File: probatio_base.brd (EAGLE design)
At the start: 50 x 50 mm, 12 parts

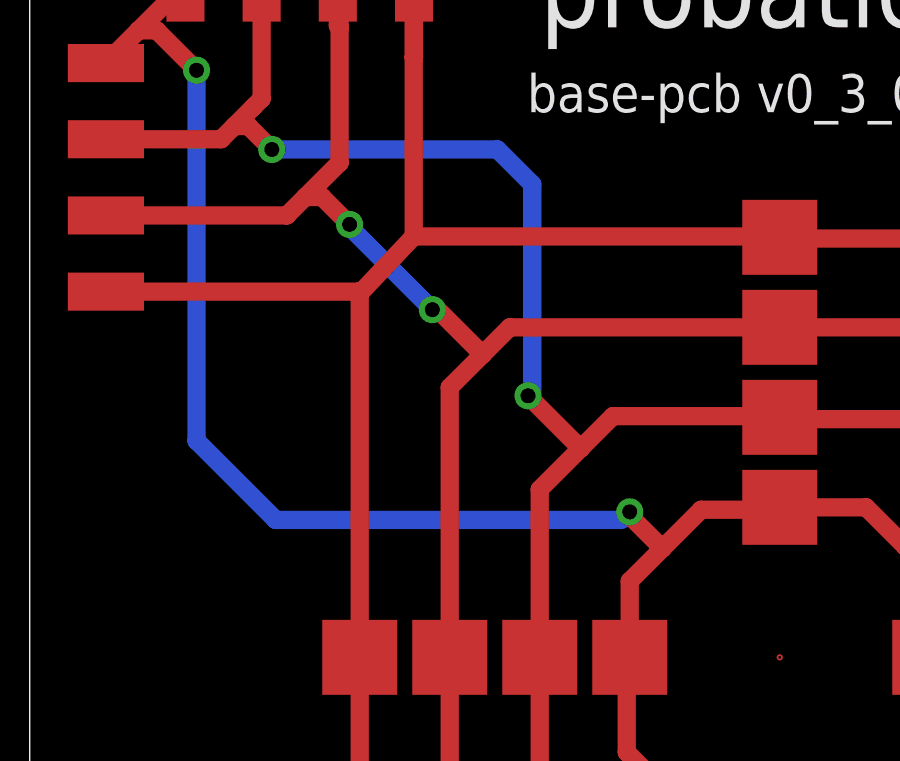
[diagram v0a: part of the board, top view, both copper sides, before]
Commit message: added batebit logo
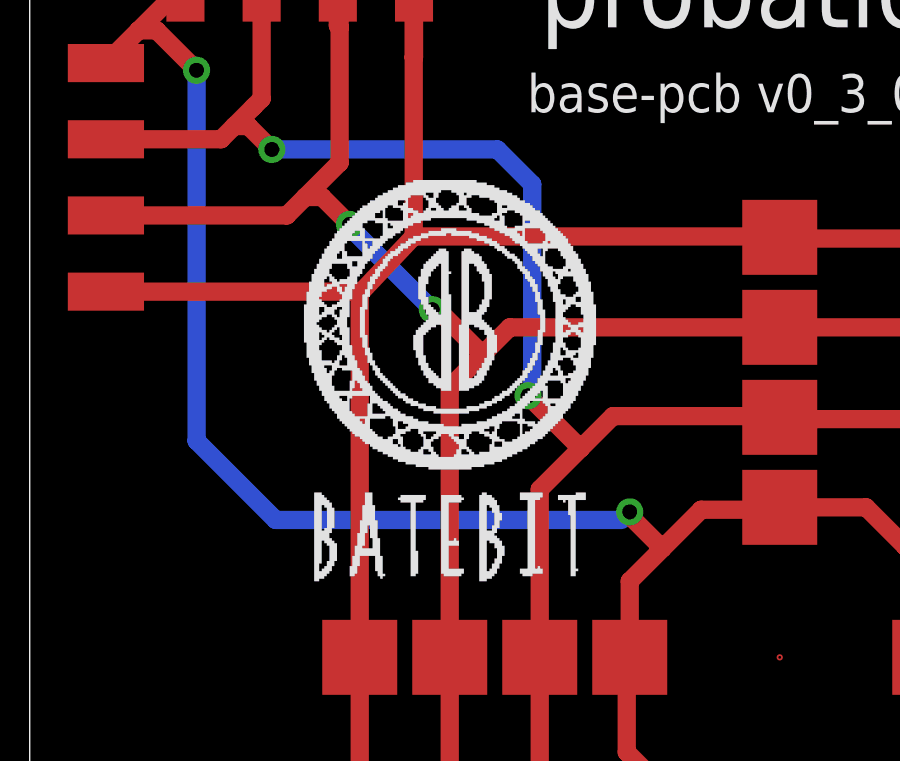
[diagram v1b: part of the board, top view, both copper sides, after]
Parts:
- added U$13: BATEBIT_PEQ, Batebit:BATEBIT_PEQ
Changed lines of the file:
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@@
 <element name="U$8" library="Batebit" package="1X04_SMD" value="M04WIRE_PAD" x="2.54" y="41"/>
 <element name="U$9" library="Batebit" package="1X04_SMD" value="M04WIRE_PAD" x="2.54" y="9" rot="R180"/>
+<element name="U$13" library="Batebit" package="BATEBIT_PEQ" value="BATEBIT_PEQ" x="14.18" y="35.45"/>
 </elements>
 <signals>
